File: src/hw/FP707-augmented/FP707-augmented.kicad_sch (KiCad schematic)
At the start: 1 part

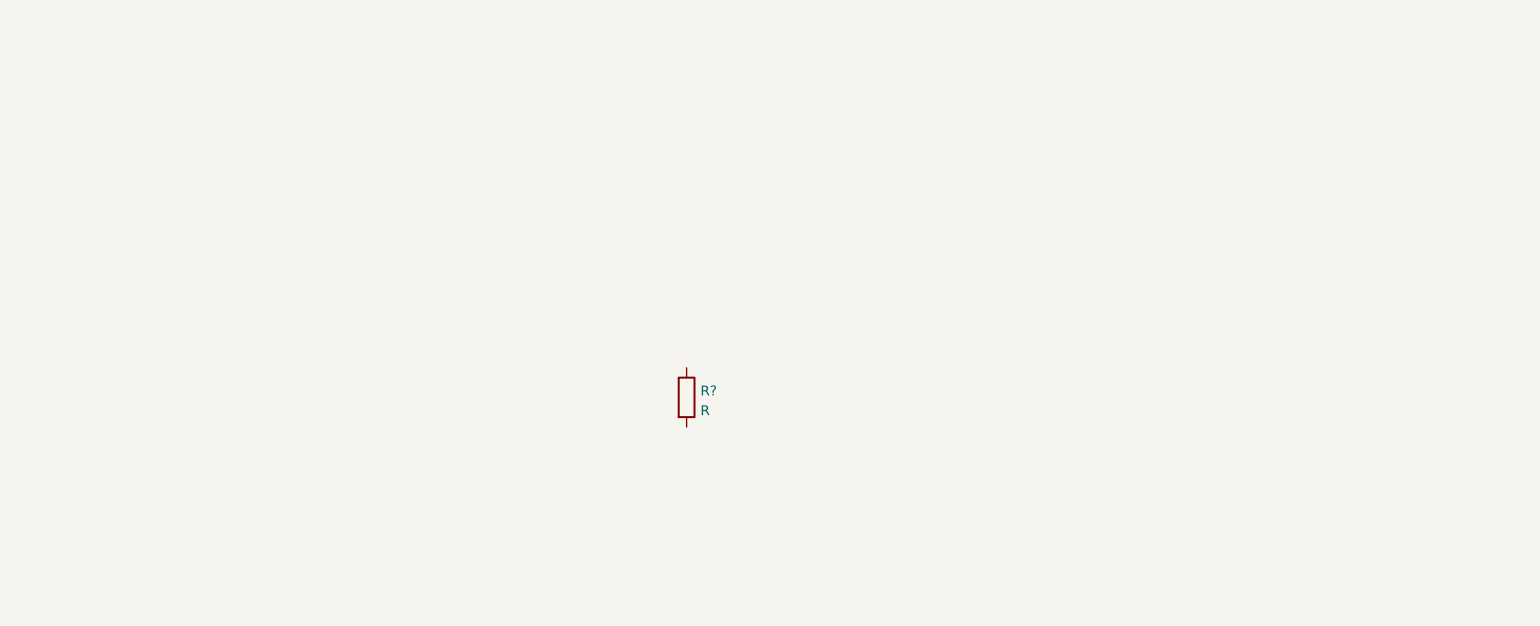
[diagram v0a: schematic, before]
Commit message: 11 - 1ere ebauche de schema
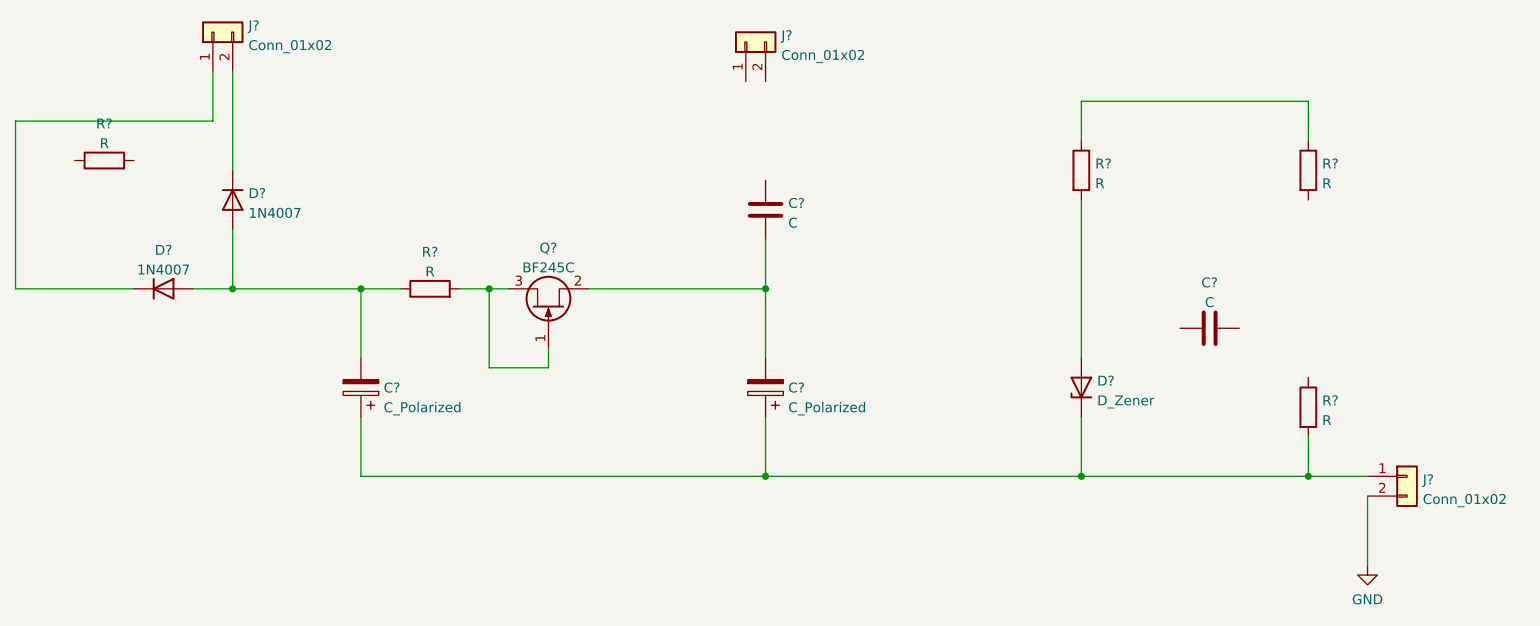
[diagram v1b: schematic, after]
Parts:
- removed R?: R, symbol Device:R
- added C? (x2): C, symbol Device:C
- added C? (x2): C_Polarized, symbol Device:C_Polarized
- added D? (x2): 1N4007, Diode_THT:D_DO-41_SOD81_P10.16mm_Horizontal, symbol Diode:1N4007
- added D?: D_Zener, symbol Device:D_Zener
- added J? (x3): Conn_01x02, symbol Connector_Generic:Conn_01x02
- added Q?: BF245C, Package_TO_SOT_THT:TO-92_Inline, symbol Transistor_FET:BF245C
- added R? (x5): R, symbol Device:R
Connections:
- new net: R?.1, R?.1
- new net: D?.2 (A), R?.2
- new net: D?.1 (K), J?.2 (Pin_2)
- new net: C?.2, D?.2 (A), D?.2 (A), R?.1
- new net: D?.1 (K), J?.1 (Pin_1)
- new net: C?.1, C?.1, D?.1 (K), J?.1 (Pin_1), R?.2
- new net: Q?.1 (G), Q?.3 (D), R?.2
- new net: C?.2, C?.2, Q?.2 (S)
- new net GND: J?.2 (Pin_2)

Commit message: 11 - add some gnd
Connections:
- net GND: now also J?.2 (Pin_2), R?.1, R?.1
- net at J?.1 (Pin_1): now also C?.1
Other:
- moved on the sheet: J?
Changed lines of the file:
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@@
   (junction (at 83.82 62.23) (diameter 0) (color 0 0 0 0)
   )
+  (junction (at 207.01 38.1) (diameter 0) (color 0 0 0 0)
+  )
   (junction (at 100.33 62.23) (diameter 0) (color 0 0 0 0)
   )
@@
   (junction (at 193.04 86.36) (diameter 0) (color 0 0 0 0)
   )
+  (wire (pts (xy 152.4 35.56) (xy 152.4 48.26))
+    (stroke (width 0) (type default) (color 0 0 0 0))
+  )
+  (wire (pts (xy 171.45 31.75) (xy 171.45 38.1))
+    (stroke (width 0) (type default) (color 0 0 0 0))
+  )
+  (wire (pts (xy 154.94 38.1) (xy 171.45 38.1))
+    (stroke (width 0) (type default) (color 0 0 0 0))
+  )
   (wire (pts (xy 83.82 62.23) (xy 100.33 62.23))
     (stroke (width 0) (type default) (color 0 0 0 0))
@@
     (stroke (width 0) (type default) (color 0 0 0 0))
   )
-  (wire (pts (xy 193.04 38.1) (xy 222.25 38.1))
+  (wire (pts (xy 193.04 38.1) (xy 207.01 38.1))
     (stroke (width 0) (type default) (color 0 0 0 0))
   )
@@
     (stroke (width 0) (type default) (color 0 0 0 0))
   )
+  (wire (pts (xy 154.94 35.56) (xy 154.94 38.1))
+    (stroke (width 0) (type default) (color 0 0 0 0))
+  )
   (wire (pts (xy 124.46 72.39) (xy 116.84 72.39))
     (stroke (width 0) (type default) (color 0 0 0 0))
@@
   )
   (wire (pts (xy 152.4 62.23) (xy 152.4 71.12))
+    (stroke (width 0) (type default) (color 0 0 0 0))
+  )
+  (wire (pts (xy 207.01 31.75) (xy 207.01 38.1))
+    (stroke (width 0) (type default) (color 0 0 0 0))
+  )
+  (wire (pts (xy 207.01 38.1) (xy 222.25 38.1))
     (stroke (width 0) (type default) (color 0 0 0 0))
   )
@@
     (pin "1")
     (pin "2")
+  )
+  (symbol (lib_id "power:GND") (at 207.01 31.75 180) (unit 1)
+    (in_bom yes) (on_board yes) (fields_autoplaced)
+    (property "Reference" "#PWR?" (id 0) (at 207.01 25.4 0)
+      (effects (font (size 1.27 1.27)) hide)
+    )
+    (property "Value" "GND" (id 1) (at 208.915 30.9138 0)
+      (effects (font (size 1.27 1.27)) (justify right))
+    )
+    (property "Footprint" "" (id 2) (at 207.01 31.75 0)
+      (effects (font (size 1.27 1.27)) hide)
+    )
+    (property "Datasheet" "" (id 3) (at 207.01 31.75 0)
+      (effects (font (size 1.27 1.27)) hide)
+    )
+    (pin "1")
   )
   (symbol (lib_id "Device:R") (at 222.25 77.47 0) (unit 1)
@@
     (pin "2")
   )
-  (symbol (lib_id "Connector_Generic:Conn_01x02") (at 149.86 30.48 90) (unit 1)
-    (in_bom yes) (on_board yes) (fields_autoplaced)
-    (property "Reference" "J?" (id 0) (at 154.432 29.6453 90)
-      (effects (font (size 1.27 1.27)) (justify right))
-    )
-    (property "Value" "Conn_01x02" (id 1) (at 154.432 32.1822 90)
-      (effects (font (size 1.27 1.27)) (justify right))
-    )
-    (property "Footprint" "" (id 2) (at 149.86 30.48 0)
-      (effects (font (size 1.27 1.27)) hide)
-    )
-    (property "Datasheet" "~" (id 3) (at 149.86 30.48 0)
+  (symbol (lib_id "Connector_Generic:Conn_01x02") (at 152.4 30.48 90) (unit 1)
+    (in_bom yes) (on_board yes) (fields_autoplaced)
+    (property "Reference" "J?" (id 0) (at 156.972 29.6453 90)
+      (effects (font (size 1.27 1.27)) (justify right))
+    )
+    (property "Value" "Conn_01x02" (id 1) (at 156.972 32.1822 90)
+      (effects (font (size 1.27 1.27)) (justify right))
+    )
+    (property "Footprint" "" (id 2) (at 152.4 30.48 0)
+      (effects (font (size 1.27 1.27)) hide)
+    )
+    (property "Datasheet" "~" (id 3) (at 152.4 30.48 0)
       (effects (font (size 1.27 1.27)) hide)
     )
@@
     (pin "2")
   )
+  (symbol (lib_id "power:GND") (at 171.45 31.75 180) (unit 1)
+    (in_bom yes) (on_board yes) (fields_autoplaced)
+    (property "Reference" "#PWR?" (id 0) (at 171.45 25.4 0)
+      (effects (font (size 1.27 1.27)) hide)
+    )
+    (property "Value" "GND" (id 1) (at 173.355 30.9138 0)
+      (effects (font (size 1.27 1.27)) (justify right))
+    )
+    (property "Footprint" "" (id 2) (at 171.45 31.75 0)
+      (effects (font (size 1.27 1.27)) hide)
+    )
+    (property "Datasheet" "" (id 3) (at 171.45 31.75 0)
+      (effects (font (size 1.27 1.27)) hide)
+    )
+    (pin "1")
+  )
   (symbol (lib_id "Connector_Generic:Conn_01x02") (at 234.95 86.36 0) (unit 1)
     (in_bom yes) (on_board yes) (fields_autoplaced)
@@
   )
   (symbol_instances
+    (path "/3c2b384c-ff5c-4218-a45b-99d6a7e9a266"
+      (reference "#PWR?") (unit 1) (value "GND") (footprint "")
+    )
     (path "/579d2668-9fff-4ead-9bc0-cdee25303e9c"
       (reference "#PWR?") (unit 1) (value "GND") (footprint "")
     )
+    (path "/88e70477-568d-4e3d-a994-e3a02f95025c"
+      (reference "#PWR?") (unit 1) (value "GND") (footprint "")
+    )

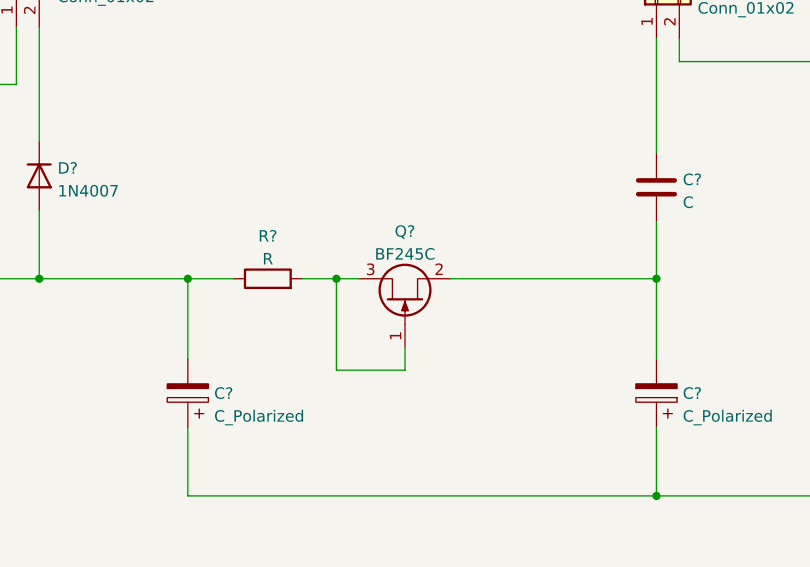
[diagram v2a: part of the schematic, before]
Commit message: BF245 to be changed into J112
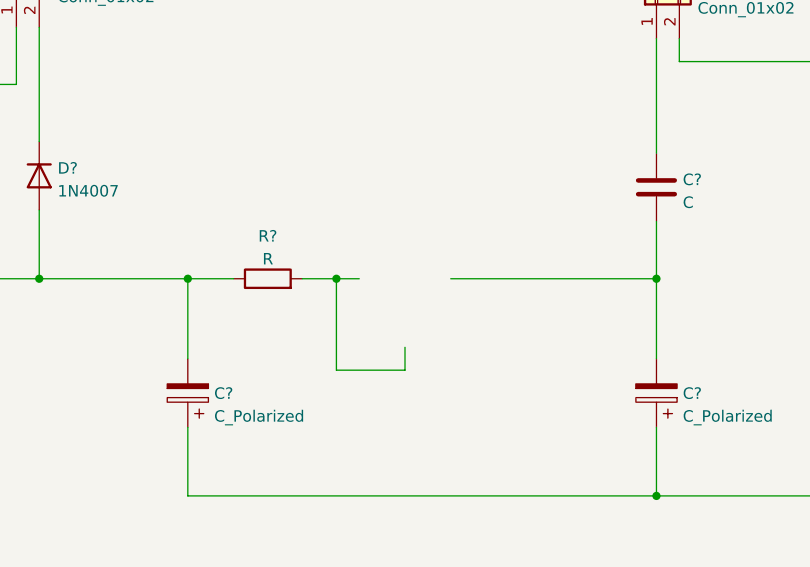
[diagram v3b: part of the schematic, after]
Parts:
- removed Q?: BF245C, Package_TO_SOT_THT:TO-92_Inline, symbol Transistor_FET:BF245C
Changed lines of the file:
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@@
     (pin "2")
-  )
-  (symbol (lib_id "Transistor_FET:BF245C") (at 124.46 64.77 90) (unit 1)
-    (in_bom yes) (on_board yes) (fields_autoplaced)
-    (property "Reference" "Q?" (id 0) (at 124.46 56.9808 90))
-    (property "Value" "BF245C" (id 1) (at 124.46 59.5177 90))
-    (property "Footprint" "Package_TO_SOT_THT:TO-92_Inline" (id 2) (at 126.365 59.69 0)
-      (effects (font (size 1.27 1.27) italic) (justify left) hide)
-    )
-    (property "Datasheet" "https://www.onsemi.com/pub/Collateral/BF245A-D.PDF" (id 3) (at 124.46 64.77 0)
-      (effects (font (size 1.27 1.27)) (justify left) hide)
-    )
-    (pin "1")
-    (pin "2")
-    (pin "3")
   )
   (symbol (lib_id "Device:R") (at 222.25 46.99 0) (unit 1)
@@
       (reference "J?") (unit 1) (value "Conn_01x02") (footprint "")
     )
-    (path "/4436c625-7cbd-4b39-b571-da224b8be55e"
-      (reference "Q?") (unit 1) (value "BF245C") (footprint "Package_TO_SOT_THT:TO-92_Inline")
-    )
     (path "/198cbc19-74e2-428f-97e4-f6e5e6d9328c"
